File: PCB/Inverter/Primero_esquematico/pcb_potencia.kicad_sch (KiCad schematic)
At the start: 0 parts

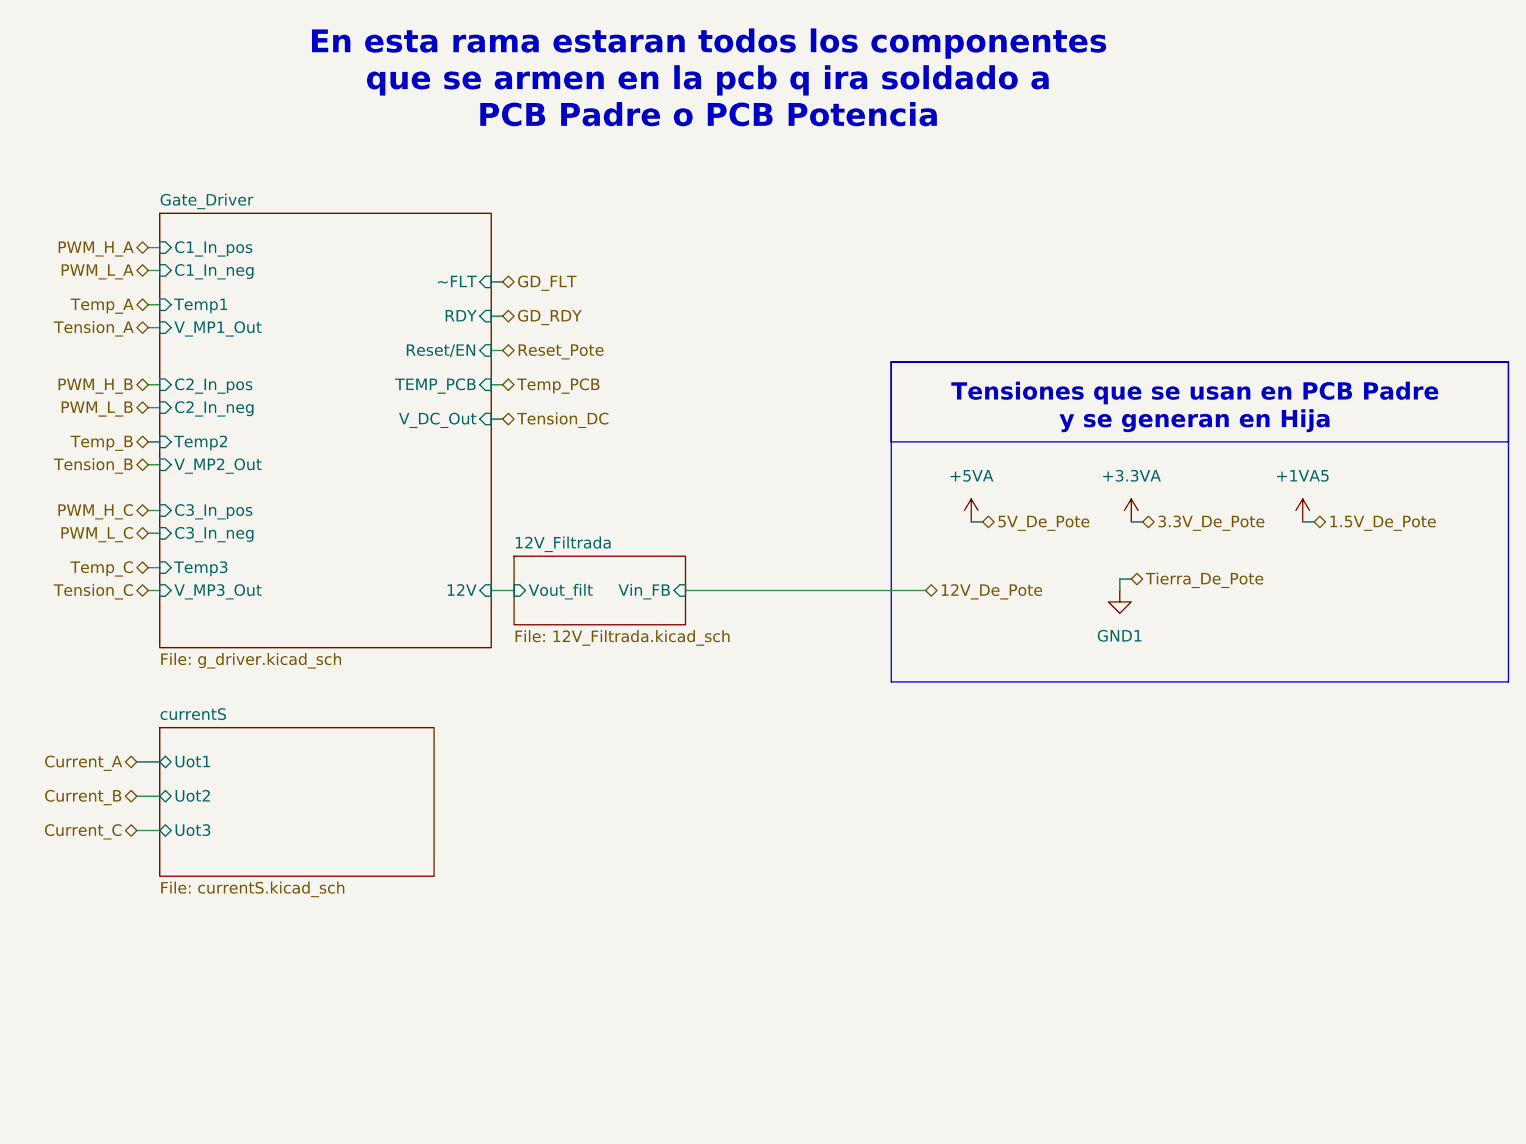
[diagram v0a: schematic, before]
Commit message: Un par de cosas q corregi del ERC pero sigue mal
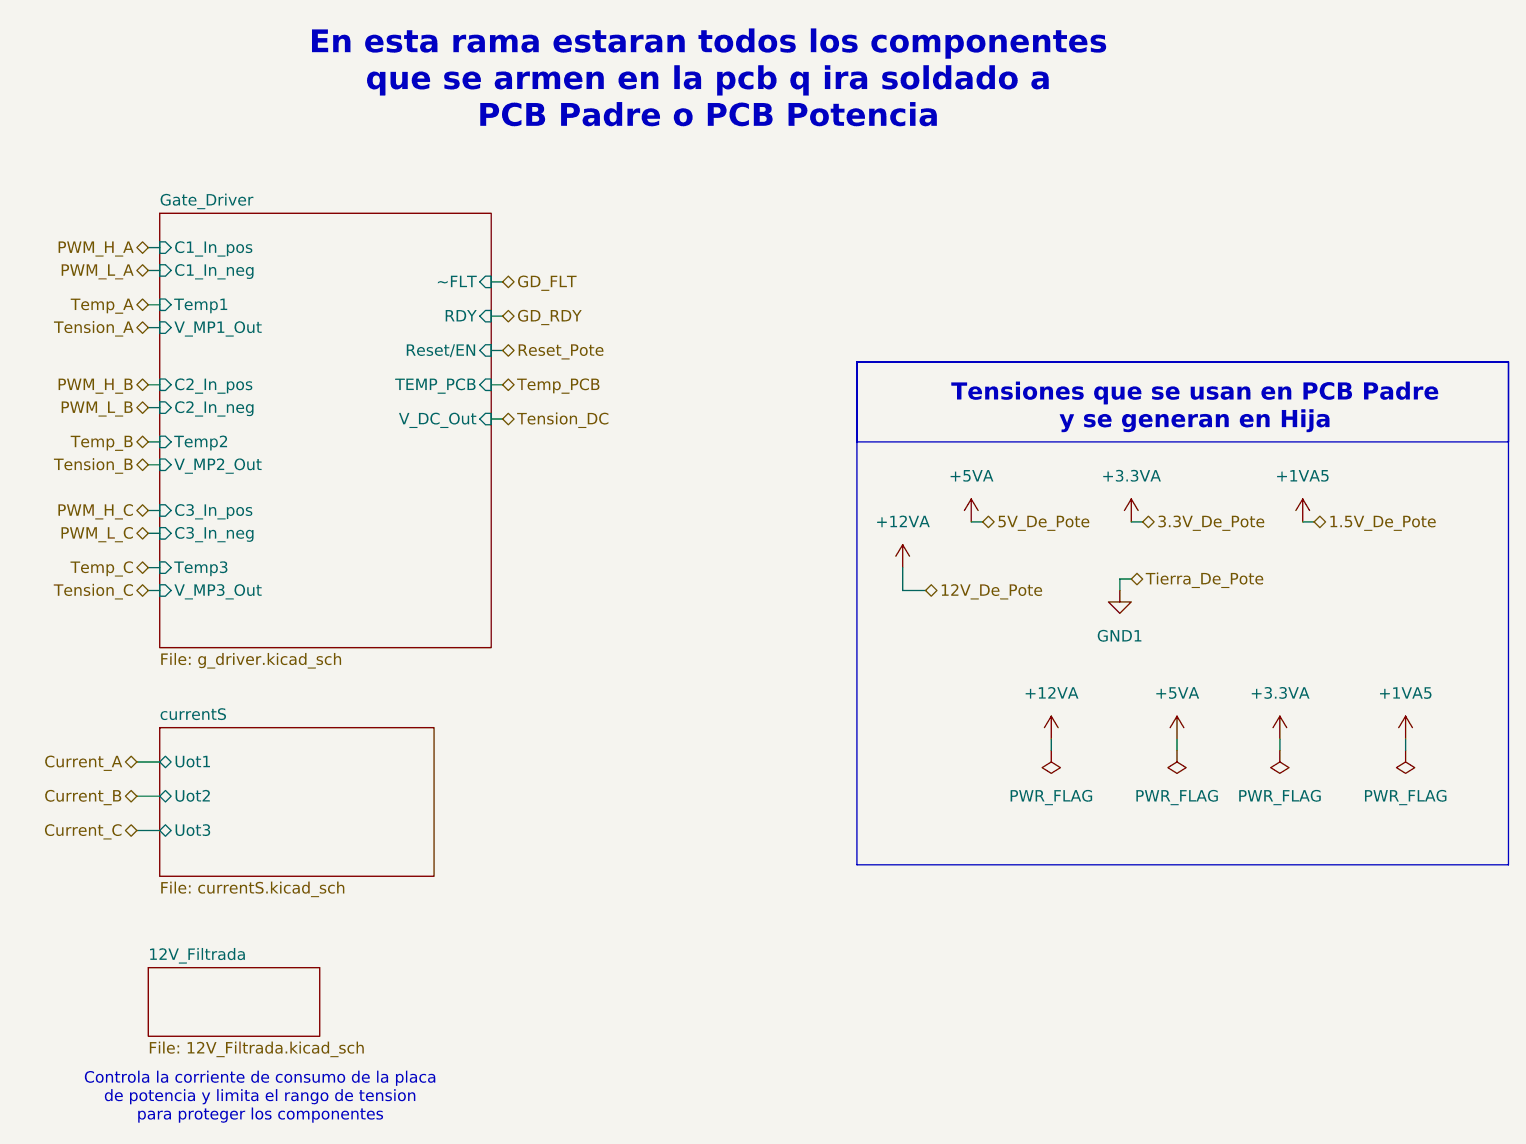
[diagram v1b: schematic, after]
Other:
- sheet 12V_Filtrada ports: added none; removed Vin_FB, Vout_filt
- sheet Gate_Driver ports: added none; removed 12V
- note added: "Controla la corriente de consumo de la placa de potencia y limita el rango de tension para proteger los componentes"

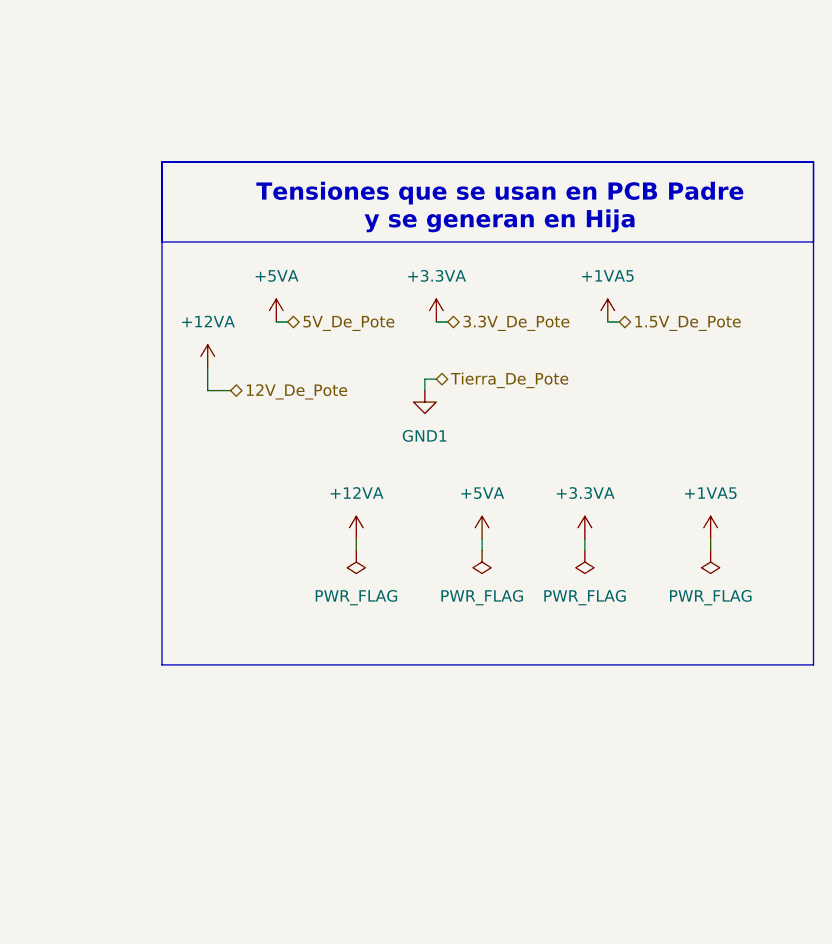
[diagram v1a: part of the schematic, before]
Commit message: Esquematico Listo
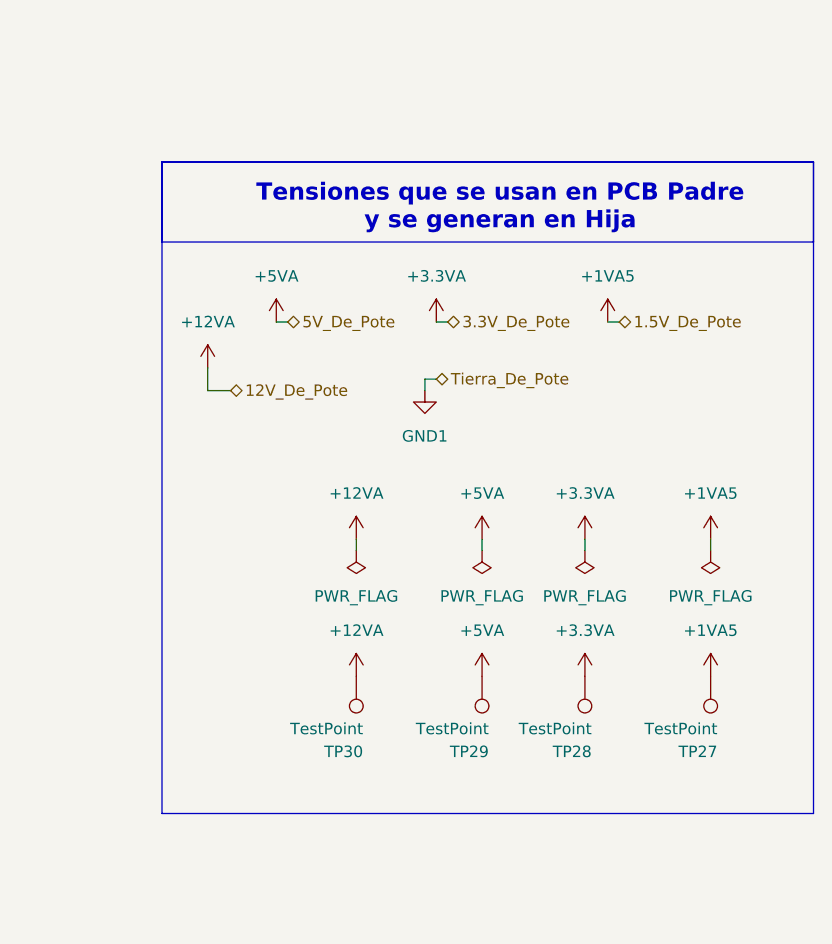
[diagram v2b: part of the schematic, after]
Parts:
- added TP27, TP28, TP29, TP30: TestPoint, TestPoint:TestPoint_Pad_D2.0mm, symbol Connector:TestPoint
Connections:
- net +12VA: now also TP30.1
- net +1VA5: now also TP27.1
- net +3.3VA: now also TP28.1
- net +5VA: now also TP29.1

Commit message: correcciones
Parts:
- TP48: renamed from TP30; footprint TestPoint:TestPoint_Pad_D2.0mm -> TestPoint:TestPoint_Pad_D1.0mm
- TP49: renamed from TP29; footprint TestPoint:TestPoint_Pad_D2.0mm -> TestPoint:TestPoint_Pad_D1.0mm
- TP50: renamed from TP28; footprint TestPoint:TestPoint_Pad_D2.0mm -> TestPoint:TestPoint_Pad_D1.0mm
- TP51: renamed from TP27; footprint TestPoint:TestPoint_Pad_D2.0mm -> TestPoint:TestPoint_Pad_D1.0mm
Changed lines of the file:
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@@
 		(dnp no)
 		(fields_autoplaced yes)
-		(property "Reference" "#PWR0222"
+		(property "Reference" "#PWR0272"
 			(at 165.1 106.68 0)
 			(hide yes)
@@
 			(project "Primero_esquematico"
 				(path "/d930f486-f6ac-489c-907e-47f2cb34cf04/d101e913-ebd1-4e08-b728-82218f47123b"
-					(reference "#PWR0222")
+					(reference "#PWR0272")
 					(unit 1)
 				)
@@
 		(dnp no)
 		(fields_autoplaced yes)
-		(property "Reference" "#PWR0276"
+		(property "Reference" "#PWR0279"
 			(at 195.58 140.97 0)
 			(hide yes)
@@
 			(project "Primero_esquematico"
 				(path "/d930f486-f6ac-489c-907e-47f2cb34cf04/d101e913-ebd1-4e08-b728-82218f47123b"
-					(reference "#PWR0276")
+					(reference "#PWR0279")
 					(unit 1)
 				)
@@
 		(dnp no)
 		(fields_autoplaced yes)
-		(property "Reference" "#PWR0223"
+		(property "Reference" "#PWR0280"
 			(at 207.01 125.73 0)
 			(hide yes)
@@
 			(project "Primero_esquematico"
 				(path "/d930f486-f6ac-489c-907e-47f2cb34cf04/d101e913-ebd1-4e08-b728-82218f47123b"
-					(reference "#PWR0223")
+					(reference "#PWR0280")
 					(unit 1)
 				)
@@
 		(dnp no)
 		(fields_autoplaced yes)
-		(property "Reference" "#FLG02"
+		(property "Reference" "#FLG027"
 			(at 207.01 125.095 0)
 			(hide yes)
@@
 			(project "Primero_esquematico"
 				(path "/d930f486-f6ac-489c-907e-47f2cb34cf04/d101e913-ebd1-4e08-b728-82218f47123b"
-					(reference "#FLG02")
+					(reference "#FLG027")
 					(unit 1)
 				)
@@
 		(dnp no)
 		(fields_autoplaced yes)
-		(property "Reference" "#PWR0278"
+		(property "Reference" "#PWR0284"
 			(at 220.98 140.97 0)
 			(hide yes)
@@
 			(project "Primero_esquematico"
 				(path "/d930f486-f6ac-489c-907e-47f2cb34cf04/d101e913-ebd1-4e08-b728-82218f47123b"
-					(reference "#PWR0278")
+					(reference "#PWR0284")
 					(unit 1)
 				)
@@
 		(in_pos_files yes)
 		(dnp no)
-		(property "Reference" "TP29"
+		(property "Reference" "TP49"
 			(at 196.342 145.542 0)
 			(show_name no)
@@
 			)
 		)
-		(property "Footprint" "TestPoint:TestPoint_Pad_D2.0mm"
+		(property "Footprint" "TestPoint:TestPoint_Pad_D1.0mm"
 			(at 190.5 137.16 0)
 			(hide yes)
@@
 			)
 		)
-		(pin "1"
-		)
-		(instances
-			(project "Primero_esquematico"
-				(path "/d930f486-f6ac-489c-907e-47f2cb34cf04/d101e913-ebd1-4e08-b728-82218f47123b"
-					(reference "TP29")
+		(property "Description_1" ""
+			(at 195.58 137.16 0)
+			(hide yes)
+			(show_name no)
+			(do_not_autoplace no)
+			(effects
+				(font
+					(size 1.27 1.27)
+				)
+			)
+		)
+		(pin "1"
+		)
+		(instances
+			(project "Primero_esquematico"
+				(path "/d930f486-f6ac-489c-907e-47f2cb34cf04/d101e913-ebd1-4e08-b728-82218f47123b"
+					(reference "TP49")
 					(unit 1)
 				)
@@
 		(dnp no)
 		(fields_autoplaced yes)
-		(property "Reference" "#FLG03"
+		(property "Reference" "#FLG028"
 			(at 220.98 125.095 0)
 			(hide yes)
@@
 			(project "Primero_esquematico"
 				(path "/d930f486-f6ac-489c-907e-47f2cb34cf04/d101e913-ebd1-4e08-b728-82218f47123b"
-					(reference "#FLG03")
+					(reference "#FLG028")
 					(unit 1)
 				)
@@
 		(dnp no)
 		(fields_autoplaced yes)
-		(property "Reference" "#FLG01"
+		(property "Reference" "#FLG026"
 			(at 195.58 125.095 0)
 			(hide yes)
@@
 			(project "Primero_esquematico"
 				(path "/d930f486-f6ac-489c-907e-47f2cb34cf04/d101e913-ebd1-4e08-b728-82218f47123b"
-					(reference "#FLG01")
+					(reference "#FLG026")
 					(unit 1)
 				)
@@
 		(in_pos_files yes)
 		(dnp no)
-		(property "Reference" "TP28"
+		(property "Reference" "TP50"
 			(at 207.772 145.542 0)
 			(show_name no)
@@
 			)
 		)
-		(property "Footprint" "TestPoint:TestPoint_Pad_D2.0mm"
+		(property "Footprint" "TestPoint:TestPoint_Pad_D1.0mm"
 			(at 201.93 137.16 0)
 			(hide yes)
@@
 			)
 		)
-		(pin "1"
-		)
-		(instances
-			(project "Primero_esquematico"
-				(path "/d930f486-f6ac-489c-907e-47f2cb34cf04/d101e913-ebd1-4e08-b728-82218f47123b"
-					(reference "TP28")
+		(property "Description_1" ""
+			(at 207.01 137.16 0)
+			(hide yes)
+			(show_name no)
+			(do_not_autoplace no)
+			(effects
+				(font
+					(size 1.27 1.27)
+				)
+			)
+		)
+		(pin "1"
+		)
+		(instances
+			(project "Primero_esquematico"
+				(path "/d930f486-f6ac-489c-907e-47f2cb34cf04/d101e913-ebd1-4e08-b728-82218f47123b"
+					(reference "TP50")
 					(unit 1)
 				)
@@
 		(dnp no)
 		(fields_autoplaced yes)
-		(property "Reference" "#PWR0228"
+		(property "Reference" "#PWR0274"
 			(at 181.61 125.73 0)
 			(hide yes)
@@
 			(project "Primero_esquematico"
 				(path "/d930f486-f6ac-489c-907e-47f2cb34cf04/d101e913-ebd1-4e08-b728-82218f47123b"
-					(reference "#PWR0228")
+					(reference "#PWR0274")
 					(unit 1)
 				)
@@
 		(dnp no)
 		(fields_autoplaced yes)
-		(property "Reference" "#PWR0114"
+		(property "Reference" "#PWR0277"
 			(at 190.5 101.6 0)
 			(hide yes)
@@
 			(project "Primero_esquematico"
 				(path "/d930f486-f6ac-489c-907e-47f2cb34cf04/d101e913-ebd1-4e08-b728-82218f47123b"
-					(reference "#PWR0114")
+					(reference "#PWR0277")
 					(unit 1)
 				)
@@
 		(dnp no)
 		(fields_autoplaced yes)
-		(property "Reference" "#PWR0136"
+		(property "Reference" "#PWR0282"
 			(at 209.55 101.6 0)
 			(hide yes)
@@
 			(project "Primero_esquematico"
 				(path "/d930f486-f6ac-489c-907e-47f2cb34cf04/d101e913-ebd1-4e08-b728-82218f47123b"
-					(reference "#PWR0136")
+					(reference "#PWR0282")
 					(unit 1)
 				)
@@
 		(dnp no)
 		(fields_autoplaced yes)
-		(property "Reference" "#PWR0158"
+		(property "Reference" "#PWR0278"
 			(at 195.58 125.73 0)
 			(hide yes)
@@
 			(project "Primero_esquematico"
 				(path "/d930f486-f6ac-489c-907e-47f2cb34cf04/d101e913-ebd1-4e08-b728-82218f47123b"
-					(reference "#PWR0158")
+					(reference "#PWR0278")
 					(unit 1)
 				)
@@
 		(dnp no)
 		(fields_autoplaced yes)
-		(property "Reference" "#PWR0155"
+		(property "Reference" "#PWR0276"
 			(at 189.23 111.76 0)
 			(hide yes)
@@
 			(project "Primero_esquematico"
 				(path "/d930f486-f6ac-489c-907e-47f2cb34cf04/d101e913-ebd1-4e08-b728-82218f47123b"
-					(reference "#PWR0155")
+					(reference "#PWR0276")
 					(unit 1)
 				)
@@
 		(dnp no)
 		(fields_autoplaced yes)
-		(property "Reference" "#PWR0224"
+		(property "Reference" "#PWR0283"
 			(at 220.98 125.73 0)
 			(hide yes)
@@
 			(project "Primero_esquematico"
 				(path "/d930f486-f6ac-489c-907e-47f2cb34cf04/d101e913-ebd1-4e08-b728-82218f47123b"
-					(reference "#PWR0224")
+					(reference "#PWR0283")
 					(unit 1)
 				)
@@
 		(in_pos_files yes)
 		(dnp no)
-		(property "Reference" "TP27"
+		(property "Reference" "TP51"
 			(at 221.742 145.542 0)
 			(show_name no)
@@
 			)
 		)
-		(property "Footprint" "TestPoint:TestPoint_Pad_D2.0mm"
+		(property "Footprint" "TestPoint:TestPoint_Pad_D1.0mm"
 			(at 215.9 137.16 0)
 			(hide yes)
@@
 			)
 		)
-		(pin "1"
-		)
-		(instances
-			(project "Primero_esquematico"
-				(path "/d930f486-f6ac-489c-907e-47f2cb34cf04/d101e913-ebd1-4e08-b728-82218f47123b"
-					(reference "TP27")
+		(property "Description_1" ""
+			(at 220.98 137.16 0)
+			(hide yes)
+			(show_name no)
+			(do_not_autoplace no)
+			(effects
+				(font
+					(size 1.27 1.27)
+				)
+			)
+		)
+		(pin "1"
+		)
+		(instances
+			(project "Primero_esquematico"
+				(path "/d930f486-f6ac-489c-907e-47f2cb34cf04/d101e913-ebd1-4e08-b728-82218f47123b"
+					(reference "TP51")
 					(unit 1)
 				)
@@
 		(dnp no)
 		(fields_autoplaced yes)
-		(property "Reference" "#PWR011"
+		(property "Reference" "#PWR0273"
 			(at 172.72 101.6 0)
 			(hide yes)
@@
 			(project "Primero_esquematico"
 				(path "/d930f486-f6ac-489c-907e-47f2cb34cf04/d101e913-ebd1-4e08-b728-82218f47123b"
-					(reference "#PWR011")
+					(reference "#PWR0273")
 					(unit 1)
 				)
@@
 		(dnp no)
 		(fields_autoplaced yes)
-		(property "Reference" "#PWR0277"
+		(property "Reference" "#PWR0281"
 			(at 207.01 140.97 0)
 			(hide yes)
@@
 			(project "Primero_esquematico"
 				(path "/d930f486-f6ac-489c-907e-47f2cb34cf04/d101e913-ebd1-4e08-b728-82218f47123b"
-					(reference "#PWR0277")
+					(reference "#PWR0281")
 					(unit 1)
 				)
@@
 		(in_pos_files yes)
 		(dnp no)
-		(property "Reference" "TP30"
+		(property "Reference" "TP48"
 			(at 182.372 145.542 0)
 			(show_name no)
@@
 			)
 		)
-		(property "Footprint" "TestPoint:TestPoint_Pad_D2.0mm"
+		(property "Footprint" "TestPoint:TestPoint_Pad_D1.0mm"
 			(at 176.53 137.16 0)
 			(hide yes)
@@
 			)
 		)
-		(pin "1"
-		)
-		(instances
-			(project "Primero_esquematico"
-				(path "/d930f486-f6ac-489c-907e-47f2cb34cf04/d101e913-ebd1-4e08-b728-82218f47123b"
-					(reference "TP30")
+		(property "Description_1" ""
+			(at 181.61 137.16 0)
+			(hide yes)
+			(show_name no)
+			(do_not_autoplace no)
+			(effects
+				(font
+					(size 1.27 1.27)
+				)
+			)
+		)
+		(pin "1"
+		)
+		(instances
+			(project "Primero_esquematico"
+				(path "/d930f486-f6ac-489c-907e-47f2cb34cf04/d101e913-ebd1-4e08-b728-82218f47123b"
+					(reference "TP48")
 					(unit 1)
 				)
@@
 		(dnp no)
 		(fields_autoplaced yes)
-		(property "Reference" "#FLG08"
+		(property "Reference" "#FLG025"
 			(at 181.61 125.095 0)
 			(hide yes)
@@
 			(project "Primero_esquematico"
 				(path "/d930f486-f6ac-489c-907e-47f2cb34cf04/d101e913-ebd1-4e08-b728-82218f47123b"
-					(reference "#FLG08")
-					(unit 1)
-				)
+					(reference "#FLG025")
+					(unit 1)
+				)

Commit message: Corregi cosas de la placa
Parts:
- removed TP48, TP49, TP50, TP51: TestPoint, TestPoint:TestPoint_Pad_D1.0mm, symbol Connector:TestPoint
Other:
- removed sheet 12V_Filtrada
- note removed: "Controla la corriente de consumo de la placa de potencia y limita el rango de tension para proteger los componentes"
- note removed: "Tensiones que se usan en PCB Padre y se generan en Hija"

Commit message: a
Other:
- sheet Gate_Driver ports: added none; removed TEMP_PCB
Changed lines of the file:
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@@
-		)
-	)
-	(hierarchical_label "Temp_PCB"
-		(shape bidirectional)
-		(at 120.65 82.55 0)
-		(effects
-			(font
-				(size 1.27 1.27)
-			)
-			(justify left)
 		)
 	)
@@
 			(effects
 				(font
-					(size 1.27 1.27)
-				)
-				(justify right)
-			)
-		)
-		(pin "TEMP_PCB" input
-			(at 119.38 82.55 0)
-			(effects
-				(font
